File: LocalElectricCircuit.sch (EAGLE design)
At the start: 26 parts, among them IC1 PIC32MX360F512L, J1 Prog. Port, U1 ADS1118, U2 ADS1118

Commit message: aware of dog pleas pet dog
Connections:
- new net N$1: IC1.RG2, X2.4
- new net N$4: X2.5
- net RB_TEMP: now also IC1.RG3
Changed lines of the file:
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@@
 <?xml version="1.0" encoding="utf-8"?>
 <!DOCTYPE eagle SYSTEM "eagle.dtd">
-<eagle version="8.7.1">
+<eagle version="7.6.0">
 <drawing>
 <settings>
 <setting alwaysvectorfont="no"/>
-<setting keepoldvectorfont="yes"/>
 <setting verticaltext="up"/>
 </settings>
-<grid distance="0.1" unitdist="inch" unit="inch" style="lines" multiple="1" display="no" altdistance="0.025" altunitdist="inch" altunit="inch"/>
+<grid distance="0.1" unitdist="inch" unit="inch" style="lines" multiple="1" display="no" altdistance="0.01" altunitdist="inch" altunit="inch"/>
 <layers>
 <layer number="1" name="Top" color="4" fill="1" visible="no" active="no"/>
@@
 <part name="C8" library="resistor" deviceset="C-US" device="C1206" value="0.1uF"/>
 <part name="C9" library="resistor" deviceset="C-US" device="C1206" value="0.1uF"/>
-<part name="PIC16" library="ic-package" library_urn="urn:adsk.eagle:library:239" deviceset="DIL20" device="" package3d_urn="urn:adsk.eagle:package:14436/1" value="pic16f689"/>
-<part name="PIC16_ICSP" library="pinhead" library_urn="urn:adsk.eagle:library:325" deviceset="PINHD-1X6" device="" package3d_urn="urn:adsk.eagle:package:22472/2"/>
+<part name="PIC16" library="ic-package" deviceset="DIL20" device="" value="pic16f689"/>
+<part name="PIC16_ICSP" library="pinhead" deviceset="PINHD-1X6" device=""/>
 <part name="C10" library="resistor" deviceset="C-US" device="C1206" value="0.1uF"/>
 <part name="C11" library="resistor" deviceset="C-US" device="C1206" value="0.01uF"/>
@@
 <segment>
 <pinref part="X2" gate="G$1" pin="8"/>
-<wire x1="130.81" y1="-7.62" x2="127" y2="-7.62" width="0.1524" layer="91"/>
 <label x="114.3" y="-7.62" size="1.778" layer="95"/>
+<pinref part="IC1" gate="G$1" pin="RG3"/>
+<wire x1="124.46" y1="43.18" x2="134.62" y2="43.18" width="0.1524" layer="91"/>
+<wire x1="134.62" y1="43.18" x2="134.62" y2="15.24" width="0.1524" layer="91"/>
+<wire x1="134.62" y1="15.24" x2="121.92" y2="15.24" width="0.1524" layer="91"/>
+<wire x1="121.92" y1="15.24" x2="121.92" y2="5.08" width="0.1524" layer="91"/>
+<wire x1="121.92" y1="5.08" x2="106.68" y2="5.08" width="0.1524" layer="91"/>
+<wire x1="106.68" y1="5.08" x2="106.68" y2="-7.62" width="0.1524" layer="91"/>
+<wire x1="106.68" y1="-7.62" x2="130.81" y2="-7.62" width="0.1524" layer="91"/>
 </segment>
 </net>
@@
 <wire x1="17.78" y1="73.66" x2="12.7" y2="73.66" width="0.1524" layer="91"/>
 <label x="-10.16" y="73.66" size="1.778" layer="95"/>
+</segment>
+</net>
+<net name="N$1" class="0">
+<segment>
+<pinref part="X2" gate="G$1" pin="4"/>
+<pinref part="IC1" gate="G$1" pin="RG2"/>
+<wire x1="124.46" y1="45.72" x2="137.16" y2="45.72" width="0.1524" layer="91"/>
+<wire x1="137.16" y1="45.72" x2="137.16" y2="17.78" width="0.1524" layer="91"/>
+<wire x1="137.16" y1="17.78" x2="124.46" y2="17.78" width="0.1524" layer="91"/>
+<wire x1="124.46" y1="17.78" x2="124.46" y2="7.62" width="0.1524" layer="91"/>
+<wire x1="124.46" y1="7.62" x2="109.22" y2="7.62" width="0.1524" layer="91"/>
+<wire x1="109.22" y1="7.62" x2="109.22" y2="-10.16" width="0.1524" layer="91"/>
+<wire x1="109.22" y1="-10.16" x2="130.81" y2="-10.16" width="0.1524" layer="91"/>
+</segment>
+</net>
+<net name="N$4" class="0">
+<segment>
+<pinref part="X2" gate="G$1" pin="5"/>
+<wire x1="130.81" y1="-15.24" x2="127" y2="-15.24" width="0.1524" layer="91"/>
 </segment>
 </net>
@@
 which will not be processed correctly with this version.
 </note>
-<note version="8.2" severity="warning">
-Since Version 8.2, EAGLE supports online libraries. The ids
-of those online libraries will not be understood (or retained)
-with this version.
-</note>
-<note version="8.3" severity="warning">
-Since Version 8.3, EAGLE supports URNs for individual library
-assets (packages, symbols, and devices). The URNs of those assets
-will not be understood (or retained) with this version.
-</note>
-<note version="8.3" severity="warning">
-Since Version 8.3, EAGLE supports the association of 3D packages
-with devices in libraries, schematics, and board files. Those 3D
-packages will not be understood (or retained) with this version.
-</note>
 </compatibility>

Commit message: Oh boy o"bertor
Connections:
- net N$1 renamed I2C_SCL
- removed net N$4: X2.5
- new net I2C_SDA: IC1.RG3, X2.5
- net RB_TEMP: no longer IC1.RG3
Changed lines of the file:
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@@
 <setting verticaltext="up"/>
 </settings>
-<grid distance="0.1" unitdist="inch" unit="inch" style="lines" multiple="1" display="no" altdistance="0.01" altunitdist="inch" altunit="inch"/>
+<grid distance="0.1" unitdist="inch" unit="inch" style="lines" multiple="1" display="no" altdistance="0.025" altunitdist="inch" altunit="inch"/>
 <layers>
 <layer number="1" name="Top" color="4" fill="1" visible="no" active="no"/>
@@
 <segment>
 <pinref part="X2" gate="G$1" pin="8"/>
+<wire x1="127" y1="-7.62" x2="130.81" y2="-7.62" width="0.1524" layer="91"/>
 <label x="114.3" y="-7.62" size="1.778" layer="95"/>
-<pinref part="IC1" gate="G$1" pin="RG3"/>
-<wire x1="124.46" y1="43.18" x2="134.62" y2="43.18" width="0.1524" layer="91"/>
-<wire x1="134.62" y1="43.18" x2="134.62" y2="15.24" width="0.1524" layer="91"/>
-<wire x1="134.62" y1="15.24" x2="121.92" y2="15.24" width="0.1524" layer="91"/>
-<wire x1="121.92" y1="15.24" x2="121.92" y2="5.08" width="0.1524" layer="91"/>
-<wire x1="121.92" y1="5.08" x2="106.68" y2="5.08" width="0.1524" layer="91"/>
-<wire x1="106.68" y1="5.08" x2="106.68" y2="-7.62" width="0.1524" layer="91"/>
-<wire x1="106.68" y1="-7.62" x2="130.81" y2="-7.62" width="0.1524" layer="91"/>
 </segment>
 </net>
@@
 </segment>
 </net>
-<net name="N$1" class="0">
+<net name="I2C_SCL" class="0">
 <segment>
 <pinref part="X2" gate="G$1" pin="4"/>
+<wire x1="127" y1="-10.16" x2="130.81" y2="-10.16" width="0.1524" layer="91"/>
+<label x="127" y="-9.525" size="1.778" layer="95" rot="R180"/>
+</segment>
+<segment>
 <pinref part="IC1" gate="G$1" pin="RG2"/>
-<wire x1="124.46" y1="45.72" x2="137.16" y2="45.72" width="0.1524" layer="91"/>
-<wire x1="137.16" y1="45.72" x2="137.16" y2="17.78" width="0.1524" layer="91"/>
-<wire x1="137.16" y1="17.78" x2="124.46" y2="17.78" width="0.1524" layer="91"/>
-<wire x1="124.46" y1="17.78" x2="124.46" y2="7.62" width="0.1524" layer="91"/>
-<wire x1="124.46" y1="7.62" x2="109.22" y2="7.62" width="0.1524" layer="91"/>
-<wire x1="109.22" y1="7.62" x2="109.22" y2="-10.16" width="0.1524" layer="91"/>
-<wire x1="109.22" y1="-10.16" x2="130.81" y2="-10.16" width="0.1524" layer="91"/>
-</segment>
-</net>
-<net name="N$4" class="0">
+<wire x1="124.46" y1="45.72" x2="134.62" y2="45.72" width="0.1524" layer="91"/>
+<label x="134.62" y="45.085" size="1.778" layer="95"/>
+</segment>
+</net>
+<net name="I2C_SDA" class="0">
 <segment>
 <pinref part="X2" gate="G$1" pin="5"/>
-<wire x1="130.81" y1="-15.24" x2="127" y2="-15.24" width="0.1524" layer="91"/>
-</segment>
-</net>
+<wire x1="127" y1="-15.24" x2="130.81" y2="-15.24" width="0.1524" layer="91"/>
+<label x="127" y="-14.605" size="1.778" layer="95" rot="R180"/>
+</segment>
+<segment>
+<pinref part="IC1" gate="G$1" pin="RG3"/>
+<wire x1="124.46" y1="43.18" x2="134.62" y2="43.18" width="0.1524" layer="91"/>
+<label x="134.62" y="42.545" size="1.778" layer="95"/>
+</segment>
+</net>

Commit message: Getting there
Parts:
- removed PIC16_ICSP: (no value), pinhead:PINHD-1X6
- added C12, C13, C14, C15, C16, C17: 0.01uF, resistor:C-USC1206
- added J3: Prog. Port, con-amp:520258-3
- added R5, R6, R8: 1k, rcl:R-US_0309/12
- added R7: 50k, rcl:R-US_M1206
- added T1: PN100, transistor:2N3704
- R4: value 50k -> 1k; device rcl:R-US_M1206 -> rcl:R-US_0309/12
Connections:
- removed net COND_ENABLE: J2.C14
- removed net COND_ENABLE_PIC: IC1.RC3
- new net CONDUCTIVITY_ENABLE_3V: IC1.RC3, R5.2
- new net CONDUCTIVITY_ENABLE_5V: J2.C14, R6.1, T1.C
- new net N$1: R5.1, T1.B
- net +3V3: now also C12.1, C13.1, C14.1, C15.1, C16.1, X1.13, X2.15, X2.8, X2.9
- net +3V3_PIC_ANALOG: now also C17.1
- net +5V: now also R6.2
- net EXT_TEMP: now also R8.1, X2.2; no longer X2.7
- net GND_3V3: now also C12.2, C13.2, C14.2, C15.2, C16.2, C17.2, J3.3, R4.2, R8.2, X1.10, X1.9, X2.12, X2.6; no longer PIC16_ICSP.3
- net GND_5V: now also T1.E
- net I2C_SCL: now also X2.13; no longer X2.4
- net I2C_SDA: now also X2.14; no longer X2.5
- net PIC16_3V3: now also J3.2, R7.1; no longer PIC16_ICSP.2, R4.2
- net PIC16_MCLR: now also J3.1, R7.2; no longer PIC16_ICSP.1, R4.1
- net PIC16_PGC: now also J3.5; no longer PIC16_ICSP.5
- net PIC16_PGD: now also J3.4; no longer PIC16_ICSP.4
- net RB_TEMP: now also R4.1, X2.1; no longer X2.8
- net U1RX: now also X2.4
- net U1TX: now also X2.5
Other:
- moved on the sheet: C1, C2, C3, C4, C5, C6, R2, R4, X2

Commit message: Started early layout
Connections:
- removed net GND_PROBE_1: J2.B11
- removed net GND_PROBE_2: J2.B12
- removed net GND_PROBE_DIFF: J2.B13
- removed net HOR_DIFF: U2.AIN0
- removed net HOR_LEFT: U2.AIN2
- removed net HOR_RIGHT: U1.AIN2
- removed net VERT_DIFF: U1.AIN1
- removed net VERT_DOWN: U2.AIN1
- removed net VERT_UP: U1.AIN0
- net GND_PROBE: now also J2.B11, J2.B12, J2.B13
- net PROBE_DIFF_HOR: now also U2.AIN0
- net PROBE_DIFF_VERT: now also U1.AIN1
- net PROBE_HOR_1_RIGHT: now also U1.AIN2
- net PROBE_HOR_2_LEFT: now also U2.AIN2
- net PROBE_VERT_1_UP: now also U1.AIN0
- net PROBE_VERT_2_DOWN: now also U2.AIN1

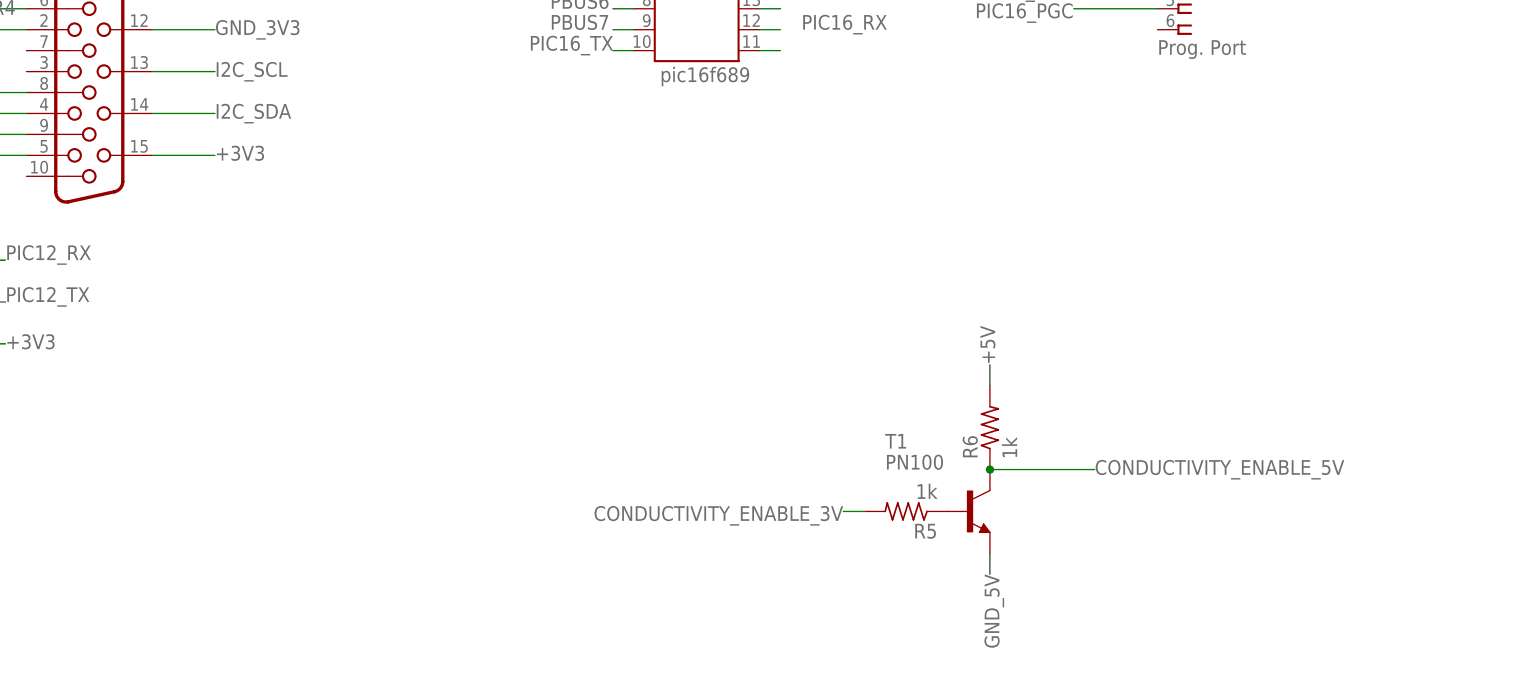
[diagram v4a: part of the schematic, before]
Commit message: Transistor circuit updated to be active high and to save power.
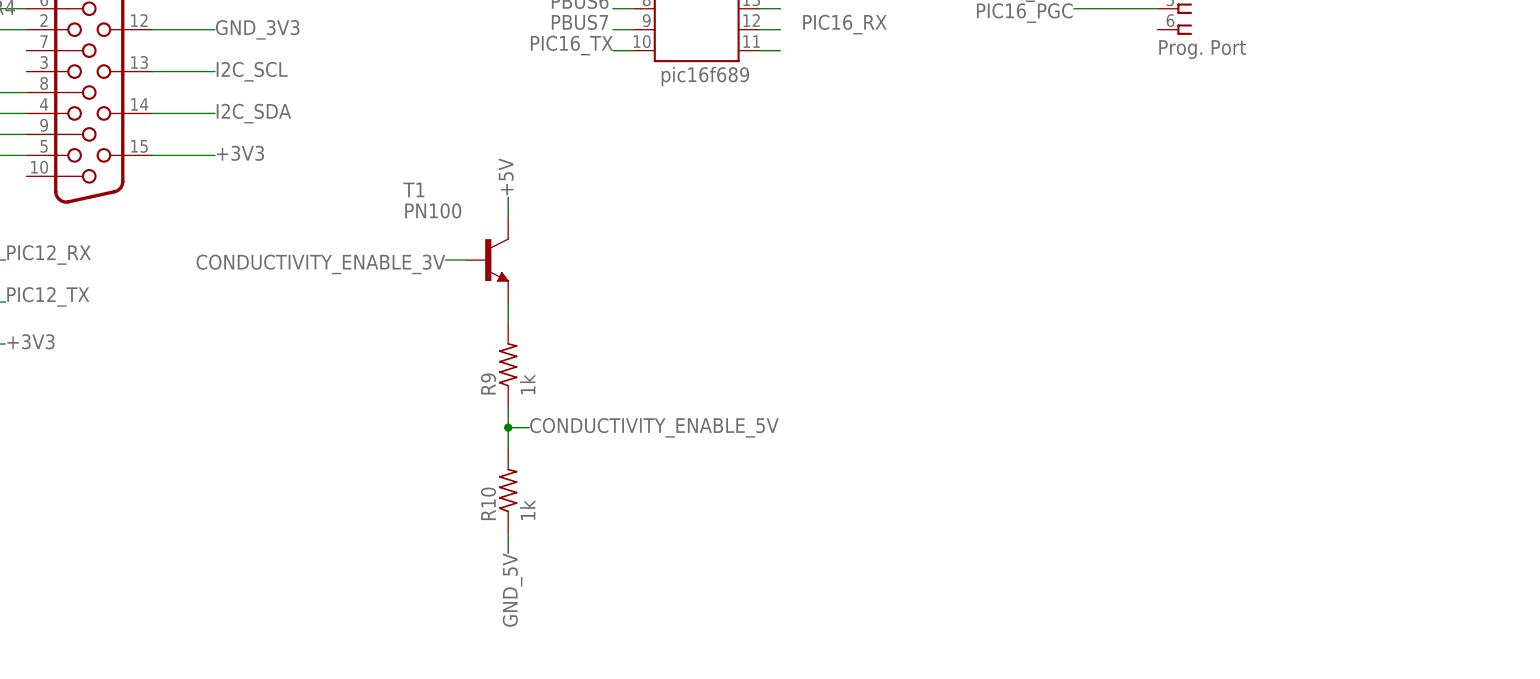
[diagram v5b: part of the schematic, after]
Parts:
- removed R5, R6: 1k, rcl:R-US_0309/12
- added R10, R9: 1k, rcl:R-US_0309/12
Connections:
- removed net N$1: R5.1, T1.B
- new net N$5: R9.2, T1.E
- net +5V: now also T1.C; no longer R6.2
- net CONDUCTIVITY_ENABLE_3V: now also T1.B; no longer R5.2
- net CONDUCTIVITY_ENABLE_5V: now also R10.2, R9.1; no longer R6.1, T1.C
- net GND_5V: now also R10.1; no longer T1.E
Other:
- moved on the sheet: T1
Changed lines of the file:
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@@
 <part name="C10" library="resistor" deviceset="C-US" device="C1206" value="0.1uF"/>
 <part name="C11" library="resistor" deviceset="C-US" device="C1206" value="0.01uF"/>
-<part name="R5" library="rcl" deviceset="R-US_" device="0309/12" value="1k"/>
 <part name="T1" library="transistor" deviceset="2N3704" device="" value="PN100"/>
-<part name="R6" library="rcl" deviceset="R-US_" device="0309/12" value="1k"/>
 <part name="J3" library="con-amp" deviceset="520258-3" device="" value="Prog. Port"/>
 <part name="R7" library="rcl" deviceset="R-US_" device="M1206" value="50k"/>
@@
 <part name="R4" library="rcl" deviceset="R-US_" device="0309/12" value="1k"/>
 <part name="R8" library="rcl" deviceset="R-US_" device="0309/12" value="1k"/>
+<part name="R9" library="rcl" deviceset="R-US_" device="0309/12" value="1k"/>
+<part name="R10" library="rcl" deviceset="R-US_" device="0309/12" value="1k"/>
 </parts>
 <sheets>
@@
 <instance part="C10" gate="G$1" x="231.14" y="25.4" rot="R90"/>
 <instance part="C11" gate="G$1" x="231.14" y="33.02" rot="R90"/>
-<instance part="R5" gate="G$1" x="259.08" y="-60.96" rot="R180"/>
-<instance part="T1" gate="G$1" x="266.7" y="-60.96"/>
-<instance part="R6" gate="G$1" x="269.24" y="-50.8" rot="R90"/>
+<instance part="T1" gate="G$1" x="208.28" y="-30.48"/>
 <instance part="J3" gate="G$1" x="292.1" y="5.08"/>
 <instance part="R7" gate="G$1" x="281.94" y="12.7" rot="R90"/>
@@
 <instance part="R4" gate="G$1" x="147.32" y="2.54" rot="R180"/>
 <instance part="R8" gate="G$1" x="139.7" y="-2.54" rot="R180"/>
+<instance part="R9" gate="G$1" x="210.82" y="-43.18" rot="R90"/>
+<instance part="R10" gate="G$1" x="210.82" y="-58.42" rot="R90"/>
 </instances>
 <busses>
@@
 </segment>
 <segment>
-<pinref part="T1" gate="G$1" pin="E"/>
-<wire x1="269.24" y1="-66.04" x2="269.24" y2="-68.58" width="0.1524" layer="91"/>
-<label x="268.605" y="-68.58" size="1.778" layer="95" rot="R270"/>
+<label x="210.185" y="-66.04" size="1.778" layer="95" rot="R270"/>
+<pinref part="R10" gate="G$1" pin="1"/>
+<wire x1="210.82" y1="-66.04" x2="210.82" y2="-63.5" width="0.1524" layer="91"/>
 </segment>
 </net>
@@
 </segment>
 <segment>
-<pinref part="R6" gate="G$1" pin="2"/>
-<wire x1="269.24" y1="-45.72" x2="269.24" y2="-43.18" width="0.1524" layer="91"/>
-<label x="269.875" y="-43.18" size="1.778" layer="95" rot="R90"/>
+<label x="211.455" y="-22.86" size="1.778" layer="95" rot="R90"/>
+<pinref part="T1" gate="G$1" pin="C"/>
+<wire x1="210.82" y1="-22.86" x2="210.82" y2="-25.4" width="0.1524" layer="91"/>
 </segment>
 </net>
@@
 </segment>
 </net>
-<net name="N$1" class="0">
-<segment>
-<pinref part="T1" gate="G$1" pin="B"/>
-<pinref part="R5" gate="G$1" pin="1"/>
-</segment>
-</net>
 <net name="CONDUCTIVITY_ENABLE_5V" class="0">
 <segment>
-<pinref part="T1" gate="G$1" pin="C"/>
-<wire x1="269.24" y1="-55.88" x2="281.94" y2="-55.88" width="0.1524" layer="91"/>
-<pinref part="R6" gate="G$1" pin="1"/>
-<junction x="269.24" y="-55.88"/>
-<label x="281.94" y="-56.515" size="1.778" layer="95"/>
+<label x="213.36" y="-51.435" size="1.778" layer="95"/>
+<wire x1="210.82" y1="-50.8" x2="213.36" y2="-50.8" width="0.1524" layer="91"/>
+<pinref part="R9" gate="G$1" pin="1"/>
+<pinref part="R10" gate="G$1" pin="2"/>
+<wire x1="210.82" y1="-48.26" x2="210.82" y2="-50.8" width="0.1524" layer="91"/>
+<junction x="210.82" y="-50.8"/>
+<wire x1="210.82" y1="-50.8" x2="210.82" y2="-53.34" width="0.1524" layer="91"/>
 </segment>
 <segment>
@@
 <net name="CONDUCTIVITY_ENABLE_3V" class="0">
 <segment>
-<pinref part="R5" gate="G$1" pin="2"/>
-<wire x1="254" y1="-60.96" x2="251.46" y2="-60.96" width="0.1524" layer="91"/>
-<label x="251.46" y="-60.325" size="1.778" layer="95" rot="R180"/>
+<label x="203.2" y="-29.845" size="1.778" layer="95" rot="R180"/>
+<pinref part="T1" gate="G$1" pin="B"/>
+<wire x1="203.2" y1="-30.48" x2="205.74" y2="-30.48" width="0.1524" layer="91"/>
 </segment>
 <segment>
@@
 </segment>
 </net>
+<net name="N$5" class="0">
+<segment>
+<pinref part="R9" gate="G$1" pin="2"/>
+<pinref part="T1" gate="G$1" pin="E"/>
+<wire x1="210.82" y1="-38.1" x2="210.82" y2="-35.56" width="0.1524" layer="91"/>
+</segment>
+</net>

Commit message: ADDED ADC RESISTORS DONT KNOW HOW TO USE GITHUB IM SORRY IN ADVANCE
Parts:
- added R11, R12, R13, R14, R5, R6: 50, rcl:R-US_M1206
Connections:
- new net N$1: R5.2, U1.DIN
- new net N$4: R6.2, U1.DOUT/DRDY
- new net N$6: R11.1, U1.SCLK
- new net N$7: R12.2, U2.DIN
- new net N$8: R13.2, U2.DOUT/DRDY
- new net N$9: R14.1, U2.SCLK
- net SCK1: now also R11.2; no longer U1.SCLK
- net SCK2: now also R14.2; no longer U2.SCLK
- net SDI1: now also R6.1; no longer U1.DOUT/DRDY
- net SDI2: now also R13.1; no longer U2.DOUT/DRDY
- net SDO1: now also R5.1; no longer U1.DIN
- net SDO2: now also R12.1; no longer U2.DIN
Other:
- moved on the sheet: U1, U2

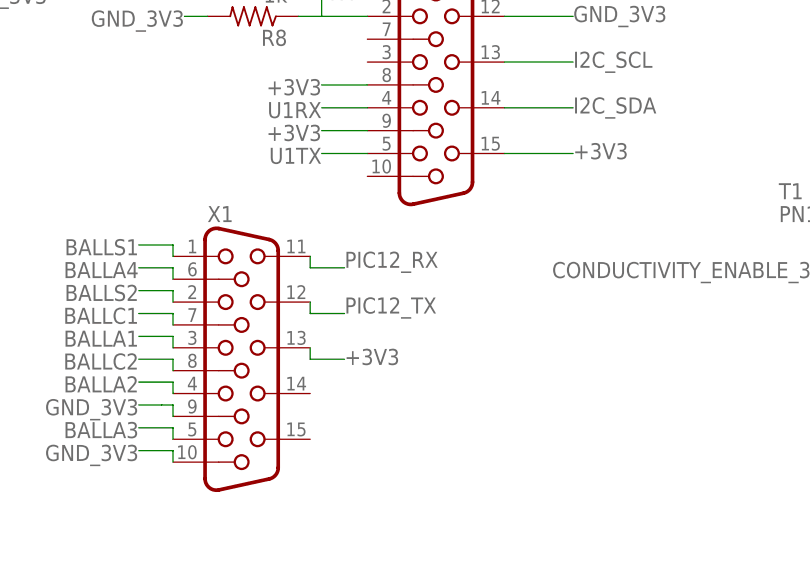
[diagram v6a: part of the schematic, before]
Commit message: CHANGED NAMES OF THE NETS LOTS OF TORNADOS COMING SOON NOW WE CAN PROGARM
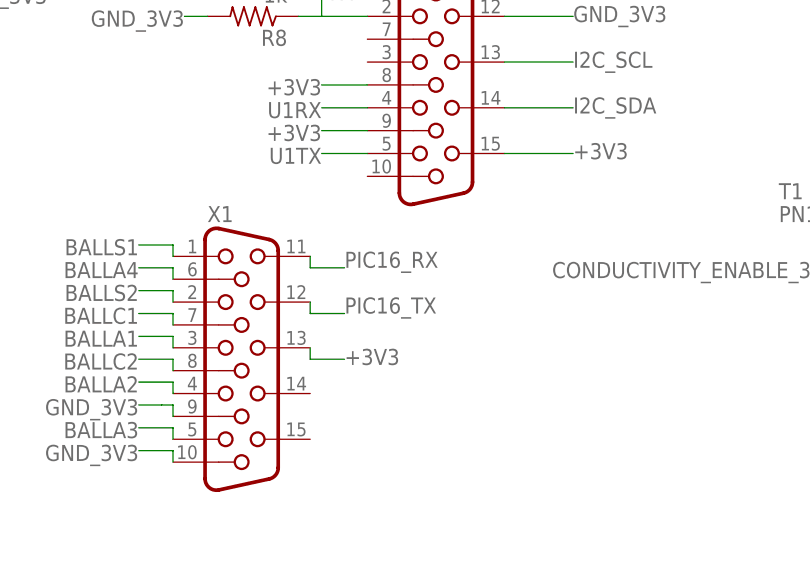
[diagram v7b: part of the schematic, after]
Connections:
- removed net PIC12_RX: X1.11
- removed net PIC12_TX: X1.12
- net PIC16_RX: now also X1.11
- net PIC16_TX: now also X1.12
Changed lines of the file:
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@@
 <label x="213.36" y="-5.08" size="1.778" layer="95"/>
+</segment>
+<segment>
+<pinref part="X1" gate="G$1" pin="12"/>
+<wire x1="146.05" y1="-34.29" x2="146.05" y2="-35.56" width="0.1524" layer="91"/>
+<wire x1="146.05" y1="-35.56" x2="149.86" y2="-35.56" width="0.1524" layer="91"/>
+<label x="149.86" y="-35.56" size="1.778" layer="95"/>
 </segment>
 </net>
@@
 <label x="246.38" y="-2.54" size="1.778" layer="95"/>
 </segment>
+<segment>
+<pinref part="X1" gate="G$1" pin="11"/>
+<wire x1="146.05" y1="-29.21" x2="146.05" y2="-30.48" width="0.1524" layer="91"/>
+<wire x1="146.05" y1="-30.48" x2="149.86" y2="-30.48" width="0.1524" layer="91"/>
+<label x="149.86" y="-30.48" size="1.778" layer="95"/>
+</segment>
 </net>
 <net name="N$20" class="0">
@@
 </segment>
 </net>
-<net name="PIC12_RX" class="0">
-<segment>
-<pinref part="X1" gate="G$1" pin="11"/>
-<wire x1="146.05" y1="-29.21" x2="146.05" y2="-30.48" width="0.1524" layer="91"/>
-<wire x1="146.05" y1="-30.48" x2="149.86" y2="-30.48" width="0.1524" layer="91"/>
-<label x="149.86" y="-30.48" size="1.778" layer="95"/>
-</segment>
-</net>
-<net name="PIC12_TX" class="0">
-<segment>
-<pinref part="X1" gate="G$1" pin="12"/>
-<wire x1="146.05" y1="-34.29" x2="146.05" y2="-35.56" width="0.1524" layer="91"/>
-<wire x1="146.05" y1="-35.56" x2="149.86" y2="-35.56" width="0.1524" layer="91"/>
-<label x="149.86" y="-35.56" size="1.778" layer="95"/>
-</segment>
-</net>
